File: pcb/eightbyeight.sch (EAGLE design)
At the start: 135 parts, among them CON1 USB_MICROSMT+THRUHULE, Q1 16MHz, SW1 SWITCH_SPDT, SW2 BRIGHTNESS, U1 MK20DN64VFM5, U10 FDG6316P, U11 FDG6316P, U12 FDG6316P, U2 ICN2026, U3 74138, U4 ICN2026, U5 MIC5219 3.3V, U6 ESP_WROOM_02, U8 MMA8653FC, U9 FDG6316P

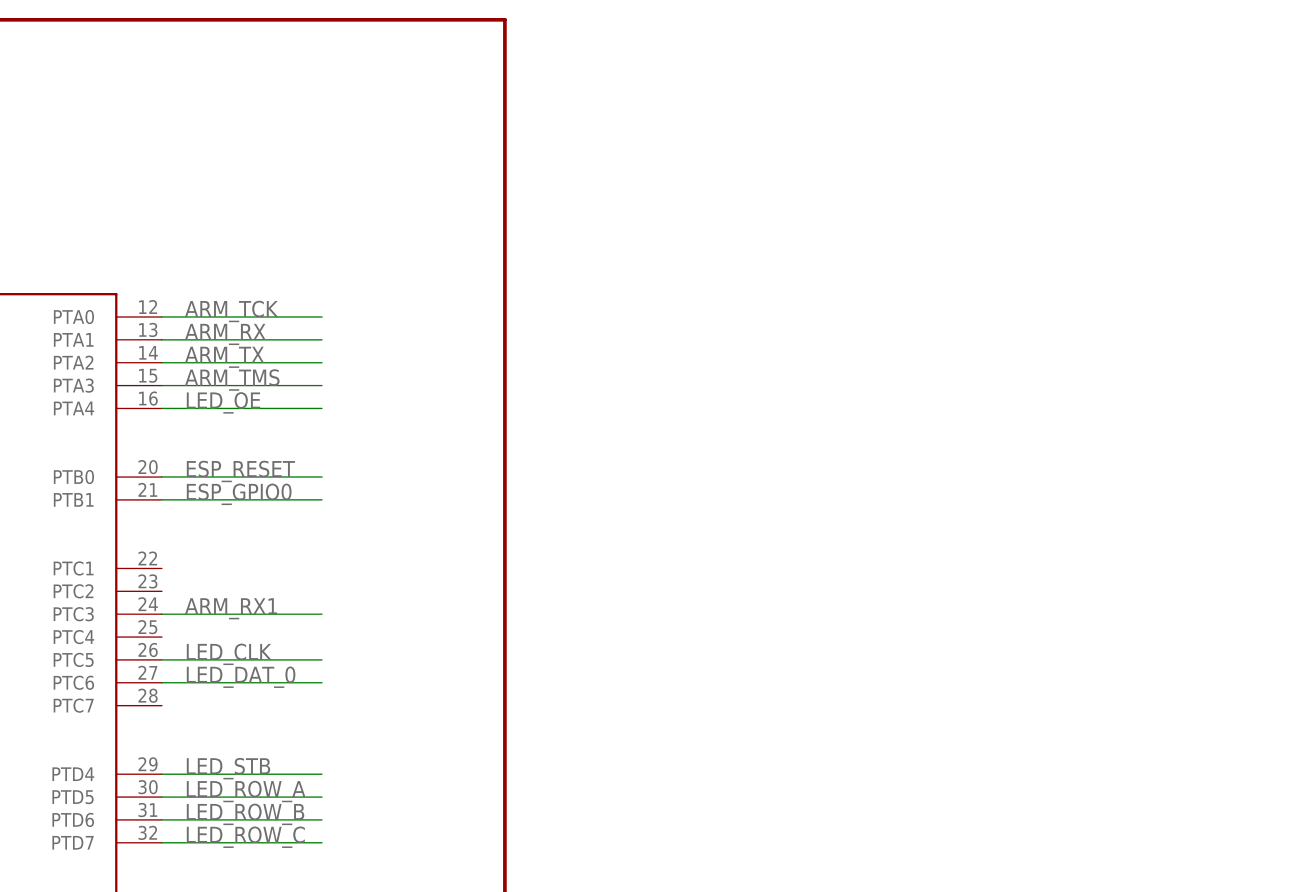
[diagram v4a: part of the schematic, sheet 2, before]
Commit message: PCB: Add LED_OE to row driver mux enable
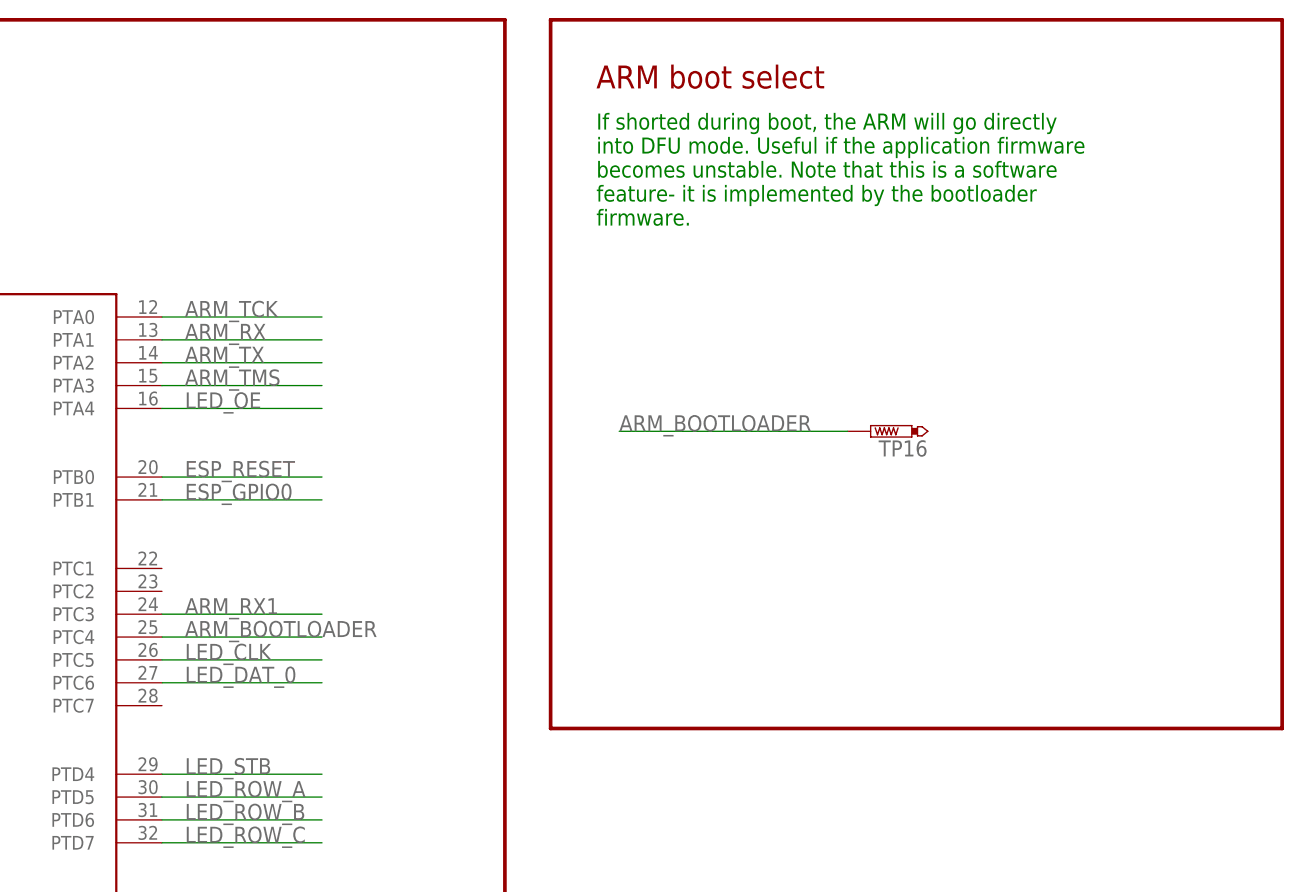
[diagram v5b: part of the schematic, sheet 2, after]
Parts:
- added TP16: PTR1B1,27, testpad:PTR1B1,27
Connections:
- new net ARM_BOOTLOADER: TP16.TP, U1.PTC4
- net GND: no longer U3A.G2A
- net LED_OE: now also U3A.G2A
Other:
- note added: "ARM boot select"
- note added: "If shorted during boot, the ARM will go directly into DFU mode. Useful if the application firmware becomes unstable. Note that this is a software feature- it is implemented by the bootloader firmware."
- note added: "Note: Based on the datasheet for the LED we are using (3528RGB4C-CA), R and B have similar luminous intensity at the same forward current so they can be driven from the same driver. Ideally each color would have an independent current setpoint, however that would require an extra drive IC"
- note added: "Note: The primary purpose for the MUX is to boost the IO signals to 5V. A secondary benefit is to reduce the number of I/O lines needed on the ARM processor."
- note added: "Revision Notes/Changelog Revision A: -Diode mod required to power over USB Revision B: -Add diodes to enable power from USB -Connect ESP reset and boot select pins to ARM for auto-programming -Connect ESP TX1 pin to ARM for LED control -Move I2C_SDA to ESP pin 12 -Connect accelerometer interrupt pin to ESP pin 13 -Remove ground planes under ESP8266 antenna area -Add jumper pad for entering boot m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"
- note removed: "Note: Based on the datasheet for the LED we are using (3528RGB4C-CA), R and B have similar luminous intensity at the same forward current so they can be driven from the same driver. Ideally each color would have an independent current setpoint."
- note removed: "Revision Notes/Changelog Revision A: -Diode mod required to power over USB Revision B: -Add diodes to enable power from USB -Connect ESP reset and boot select pins to ARM for auto-programming -Connect ESP TX1 pin to ARM for LED control -Move I2C_SDA to ESP pin 12 -Connect accelerometer interrupt pin to ESP pin 13 -Remove ground planes under ESP8266 antenna area TODO: -Add jumper pad for entering 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"
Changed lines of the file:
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@@
 <part name="3V3" library="supply1" deviceset="+3V3" device=""/>
 <part name="R12" library="adafruit" deviceset="R-US_" device="R0402" value="10k"/>
+<part name="TP16" library="testpad" deviceset="PTR1" device="B1,27"/>
 </parts>
 <sheets>
@@
 -Connect accelerometer interrupt pin to ESP pin 13
 -Remove ground planes under ESP8266 antenna area
+-Add jumper pad for entering boot mode on ARM processor
+-Hook LED_OE or similar to the row driver MUX
 TODO:
--Add jumper pad for entering boot mode on ARM processor
--Hook LED_OE or similar to the row driver MUX (if 3.3v compatible)
 -Break out some IO on ESP for expansion
 -Will smaller diode sizes work?
@@
 ESP_RESET is virtually connected to RTS
 ESP_GPIO0 is virtually connected to DTR</text>
+<text x="193.04" y="228.6" size="1.778" layer="91">If shorted during boot, the ARM will go directly
+into DFU mode. Useful if the application firmware
+becomes unstable. Note that this is a software
+feature- it is implemented by the bootloader
+firmware.</text>
+<text x="193.04" y="243.84" size="2.54" layer="94">ARM boot select</text>
+<wire x1="187.96" y1="251.46" x2="269.24" y2="251.46" width="0.4064" layer="94"/>
+<wire x1="187.96" y1="172.72" x2="187.96" y2="251.46" width="0.4064" layer="94"/>
+<wire x1="269.24" y1="172.72" x2="269.24" y2="251.46" width="0.4064" layer="94"/>
+<wire x1="187.96" y1="172.72" x2="269.24" y2="172.72" width="0.4064" layer="94"/>
 </plain>
 <instances>
@@
 <attribute name="VALUE" x="91.44" y="227.33" size="1.778" layer="96"/>
 </instance>
+<instance part="TP16" gate="G$1" x="223.52" y="205.74" rot="R90"/>
 </instances>
 <busses>
@@
 <wire x1="144.78" y1="185.42" x2="162.56" y2="185.42" width="0.1524" layer="91"/>
 <label x="147.32" y="185.42" size="1.778" layer="95"/>
+</segment>
+</net>
+<net name="ARM_BOOTLOADER" class="0">
+<segment>
+<pinref part="TP16" gate="G$1" pin="TP"/>
+<wire x1="220.98" y1="205.74" x2="195.58" y2="205.74" width="0.1524" layer="91"/>
+<label x="195.58" y="205.74" size="1.778" layer="95"/>
+</segment>
+<segment>
+<pinref part="U1" gate="G$1" pin="PTC4"/>
+<wire x1="162.56" y1="182.88" x2="144.78" y2="182.88" width="0.1524" layer="91"/>
+<label x="147.32" y="182.88" size="1.778" layer="95"/>
 </segment>
 </net>
@@
 at the same forward current so they can be driven from the
 same driver. Ideally each color would have an independent
-current setpoint.</text>
+current setpoint, however that would require an extra drive
+IC</text>
+<text x="109.22" y="22.86" size="1.778" layer="91">Note: The primary purpose for the MUX is to boost the
+IO signals to 5V. A secondary benefit is to reduce the
+number of I/O lines needed on the ARM processor.</text>
 </plain>
 <instances>
@@
 <wire x1="50.8" y1="33.02" x2="48.26" y2="33.02" width="0.1524" layer="91"/>
 <wire x1="48.26" y1="33.02" x2="48.26" y2="30.48" width="0.1524" layer="91"/>
-<pinref part="U3" gate="A" pin="G2A"/>
-<wire x1="50.8" y1="35.56" x2="48.26" y2="35.56" width="0.1524" layer="91"/>
-<wire x1="48.26" y1="35.56" x2="48.26" y2="33.02" width="0.1524" layer="91"/>
-<junction x="48.26" y="33.02"/>
 </segment>
 <segment>
@@
 <label x="17.78" y="165.1" size="1.778" layer="95" rot="R90"/>
 </segment>
-</net>
+<segment>
+<pinref part="U3" gate="A" pin="G2A"/>
+<wire x1="50.8" y1="35.56" x2="33.02" y2="35.56" width="0.1524" layer="91"/>
+<label x="33.02" y="35.56" size="1.778" layer="95"/>
+</segment>
+</net>

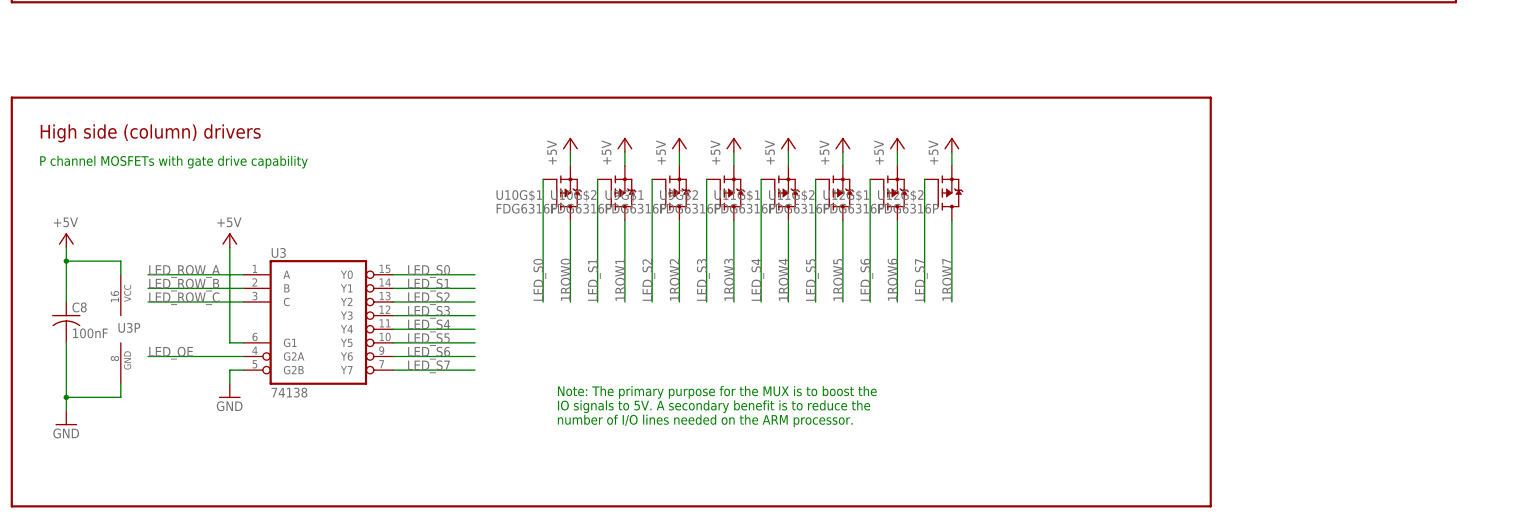
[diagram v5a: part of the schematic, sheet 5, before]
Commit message: Add LED_HS_EN. Increase number of vias on power lines
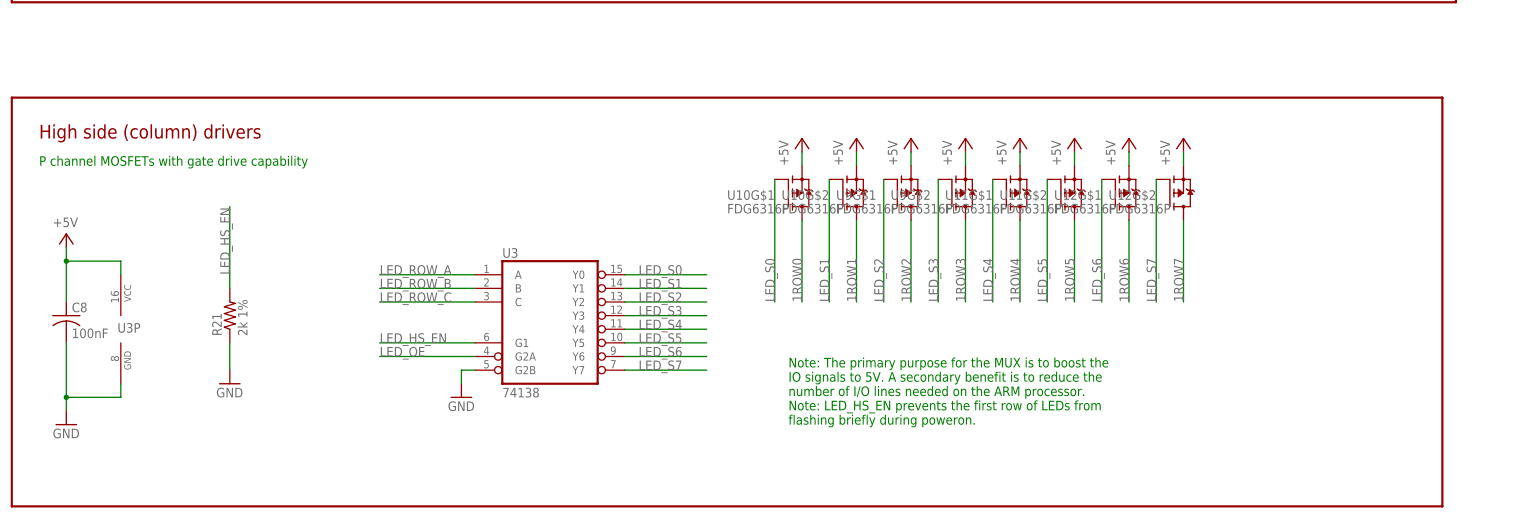
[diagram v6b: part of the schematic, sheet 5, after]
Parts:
- added R21: 2k 1%, adafruit:R-US_R0402
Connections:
- net ESP_EXP_3 renamed ESP_EXP_2
- new net LED_HS_EN: R21.2, U1.PTC1, U3A.G1
- net +5V: no longer U3A.G1
- net GND: now also R21.1
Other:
- note added: "Note: The primary purpose for the MUX is to boost the IO signals to 5V. A secondary benefit is to reduce the number of I/O lines needed on the ARM processor. Note: LED_HS_EN prevents the first row of LEDs from flashing briefly during poweron."
- note removed: "Note: The primary purpose for the MUX is to boost the IO signals to 5V. A secondary benefit is to reduce the number of I/O lines needed on the ARM processor."
- moved on the sheet: U10G$1, U10G$2, U11G$1, U11G$2, U12G$1, U12G$2, U3, U9G$1, U9G$2

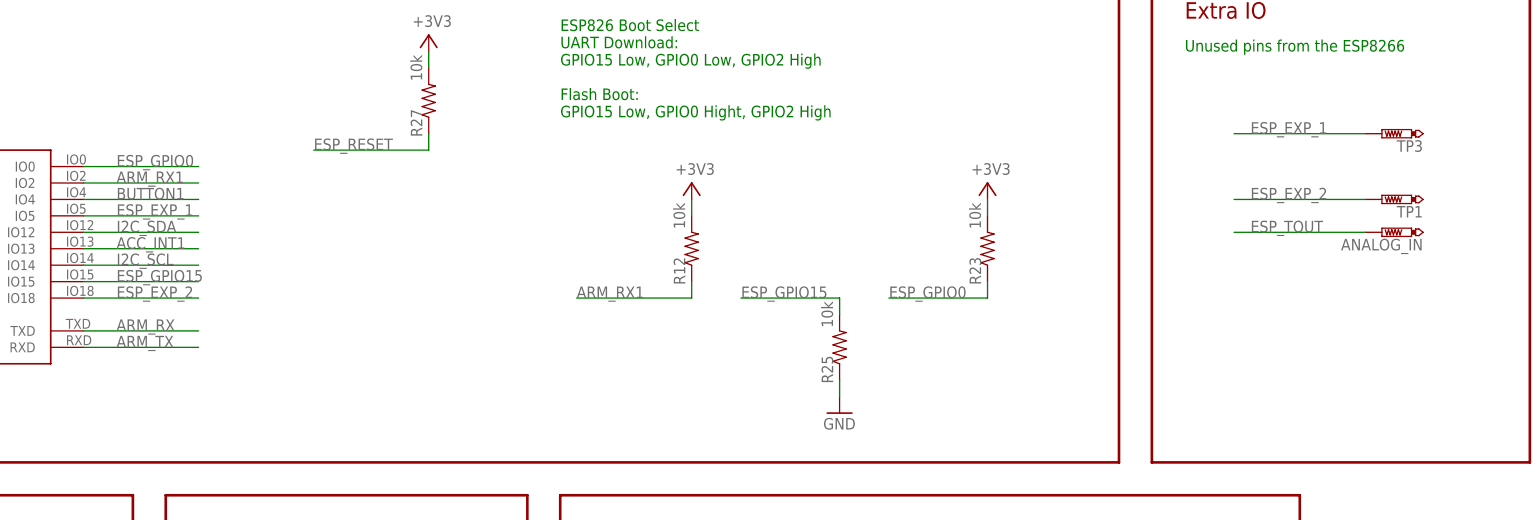
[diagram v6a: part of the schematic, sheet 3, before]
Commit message: Finish placing power diodes and clear DRC errors
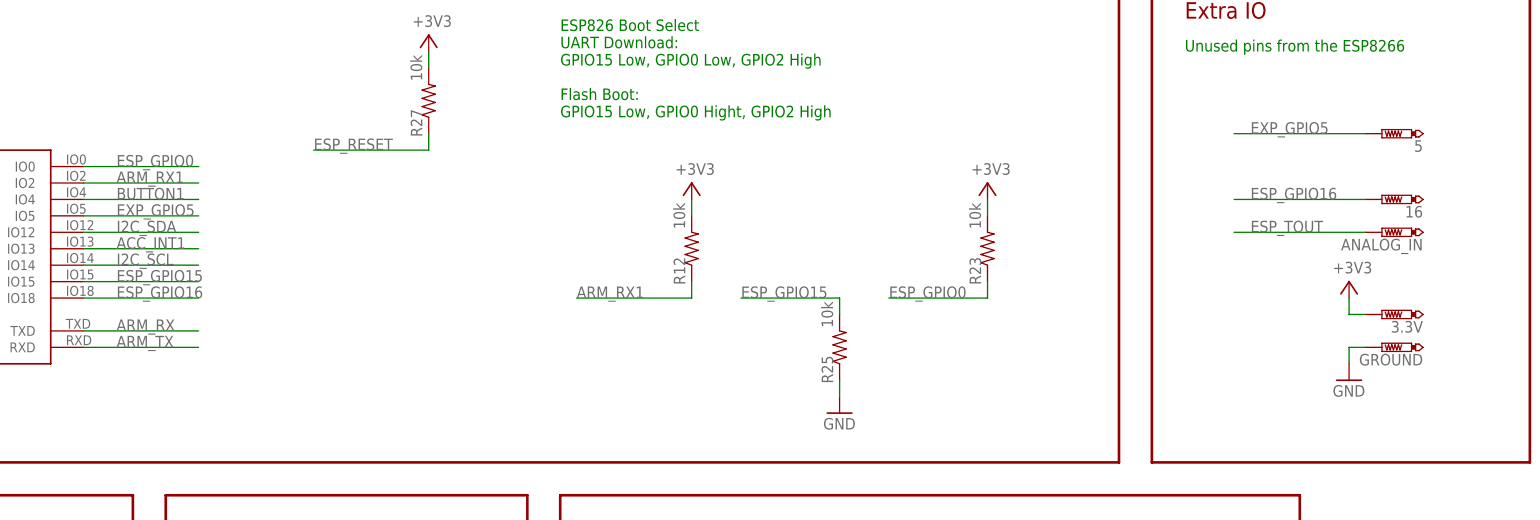
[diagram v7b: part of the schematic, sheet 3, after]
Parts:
- added 3.3V, GROUND: PTR1B2,54, testpad:PTR1B2,54
- renumbered TP1 to 16, TP3 to 5
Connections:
- net ESP_EXP_1 renamed EXP_GPIO5
- net ESP_EXP_2 renamed ESP_GPIO16
- net N$1 renamed +5V_SWITCH
- net N$4 renamed +5V_BLEED
- net +3V3: now also 3.3V.TP
- net GND: now also GROUND.TP
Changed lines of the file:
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@@
 <part name="R11" library="adafruit" deviceset="R-US_" device="R0805" value="50"/>
 <part name="GND43" library="SparkFun-Aesthetics" deviceset="GND" device=""/>
-<part name="TP1" library="testpad" deviceset="PTR1" device="B2,54"/>
-<part name="TP3" library="testpad" deviceset="PTR1" device="B2,54"/>
+<part name="16" library="testpad" deviceset="PTR1" device="B2,54"/>
+<part name="5" library="testpad" deviceset="PTR1" device="B2,54"/>
 <part name="ANALOG_IN" library="testpad" deviceset="PTR1" device="B2,54"/>
 <part name="3V3" library="supply1" deviceset="+3V3" device=""/>
@@
 <part name="R21" library="adafruit" deviceset="R-US_" device="R0402" value="2k 1%"/>
 <part name="GND35" library="SparkFun-Aesthetics" deviceset="GND" device=""/>
+<part name="3.3V" library="testpad" deviceset="PTR1" device="B2,54"/>
+<part name="GROUND" library="testpad" deviceset="PTR1" device="B2,54"/>
+<part name="3V7" library="supply1" deviceset="+3V3" device=""/>
+<part name="GND44" library="supply1" deviceset="GND" device=""/>
 </parts>
 <sheets>
@@
 -Add jumper pad for entering boot mode on ARM processor
 -Hook LED_OE or similar to the row driver MUX
+-Bring unused ESP pins to pads
 TODO:
--Break out some IO on ESP for expansion
--Will smaller diode sizes work?
+-Implement more user friendly expansion pads for the ESP
 -Cosmetic: ESP8266 GPIO 18mislabeled, should be 16
--With LED_HS_EN, should LED_OE still be connected to the mux?</text>
+-With LED_HS_EN, should LED_OE still be connected to the mux?
+-Characterize the power situation</text>
 <text x="129.54" y="358.14" size="10.16" layer="91" align="bottom-center">EightByEight Blinky Badge</text>
 <text x="129.54" y="345.44" size="6.4516" layer="91" align="bottom-center">Copyright 2016 Blinkinlabs, LLC</text>
@@
 <attribute name="VALUE" x="17.78" y="148.59" size="1.778" layer="96"/>
 </instance>
-<instance part="TP1" gate="G$1" x="287.02" y="215.9" rot="R90"/>
-<instance part="TP3" gate="G$1" x="287.02" y="226.06" rot="R90"/>
+<instance part="16" gate="G$1" x="287.02" y="215.9" rot="R90"/>
+<instance part="5" gate="G$1" x="287.02" y="226.06" rot="R90"/>
 <instance part="ANALOG_IN" gate="G$1" x="287.02" y="210.82" rot="R90"/>
 <instance part="3V3" gate="G$1" x="180.34" y="218.44" smashed="yes">
@@
 <attribute name="VALUE" x="179.324" y="211.328" size="1.778" layer="96" rot="R90"/>
 </instance>
+<instance part="3.3V" gate="G$1" x="287.02" y="198.12" rot="R90"/>
+<instance part="GROUND" gate="G$1" x="287.02" y="193.04" rot="R90"/>
+<instance part="3V7" gate="G$1" x="281.94" y="203.2" smashed="yes">
+<attribute name="VALUE" x="279.4" y="204.47" size="1.778" layer="96"/>
+</instance>
+<instance part="GND44" gate="1" x="281.94" y="187.96"/>
 </instances>
 <busses>
@@
 <pinref part="GND31" gate="1" pin="GND"/>
 </segment>
+<segment>
+<pinref part="GROUND" gate="G$1" pin="TP"/>
+<wire x1="284.48" y1="193.04" x2="281.94" y2="193.04" width="0.1524" layer="91"/>
+<wire x1="281.94" y1="193.04" x2="281.94" y2="190.5" width="0.1524" layer="91"/>
+<pinref part="GND44" gate="1" pin="GND"/>
+</segment>
 </net>
 <net name="+3V3" class="0">
@@
 <wire x1="180.34" y1="215.9" x2="180.34" y2="213.36" width="0.1524" layer="91"/>
 </segment>
+<segment>
+<pinref part="3.3V" gate="G$1" pin="TP"/>
+<wire x1="284.48" y1="198.12" x2="281.94" y2="198.12" width="0.1524" layer="91"/>
+<wire x1="281.94" y1="198.12" x2="281.94" y2="200.66" width="0.1524" layer="91"/>
+<pinref part="3V7" gate="G$1" pin="+3V3"/>
+</segment>
 </net>
 <net name="ARM_TX" class="0">
@@
 </segment>
 </net>
-<net name="ESP_EXP_1" class="0">
+<net name="EXP_GPIO5" class="0">
 <segment>
 <pinref part="U6" gate="G$1" pin="IO5"/>
@@
 </segment>
 <segment>
-<pinref part="TP3" gate="G$1" pin="TP"/>
+<pinref part="5" gate="G$1" pin="TP"/>
 <wire x1="284.48" y1="226.06" x2="264.16" y2="226.06" width="0.1524" layer="91"/>
 <label x="266.7" y="226.06" size="1.778" layer="95"/>
 </segment>
 </net>
-<net name="ESP_EXP_2" class="0">
+<net name="ESP_GPIO16" class="0">
 <segment>
 <pinref part="U6" gate="G$1" pin="IO18"/>
@@
 </segment>
 <segment>
-<pinref part="TP1" gate="G$1" pin="TP"/>
+<pinref part="16" gate="G$1" pin="TP"/>
 <wire x1="284.48" y1="215.9" x2="264.16" y2="215.9" width="0.1524" layer="91"/>
 <label x="266.7" y="215.9" size="1.778" layer="95"/>
@@
 </segment>
 </net>
-<net name="N$1" class="0">
+<net name="+5V_SWITCH" class="0">
 <segment>
 <pinref part="D2" gate="G$1" pin="C"/>
@@
 </segment>
 </net>
-<net name="N$4" class="0">
+<net name="+5V_BLEED" class="0">
 <segment>
 <pinref part="SW1" gate="G$1" pin="O"/>
